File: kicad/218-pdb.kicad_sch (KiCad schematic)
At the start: 73 parts, among them J1 Conn_01x03, J10 Conn_01x03, J11 Conn_01x03, J12 Conn_01x03, J13 Conn_01x03, J14 Conn_01x03, J15 Conn_01x03, J16 Conn_01x03, J17 Conn_01x03, J18 Conn_01x03, J19 Conn_01x03, J2 Conn_01x03, J20 Conn_01x03, J21 Conn_01x03, J22 Conn_01x03, J23 Conn_01x03, J24 Conn_01x03, J25 Conn_01x04_Pin, J26 Conn_01x04_Pin, J27 Conn_01x04_Pin, J28 Conn_01x04_Pin, J29 14 V molex, J3 Conn_01x03, J30 14 V molex, J31 14 V molex, J32 14 V molex, J33 external 5V, J34 battery, J35 battery, J4 Conn_01x03, J5 Conn_01x03, J6 Conn_01x03, J7 Conn_01x03, J8 Conn_01x03, J9 Conn_01x03, SW1 5V switch, U1 DC-DC buck, U2 DC-DC buck, U3 LD1117V33, U4 LD1117V33

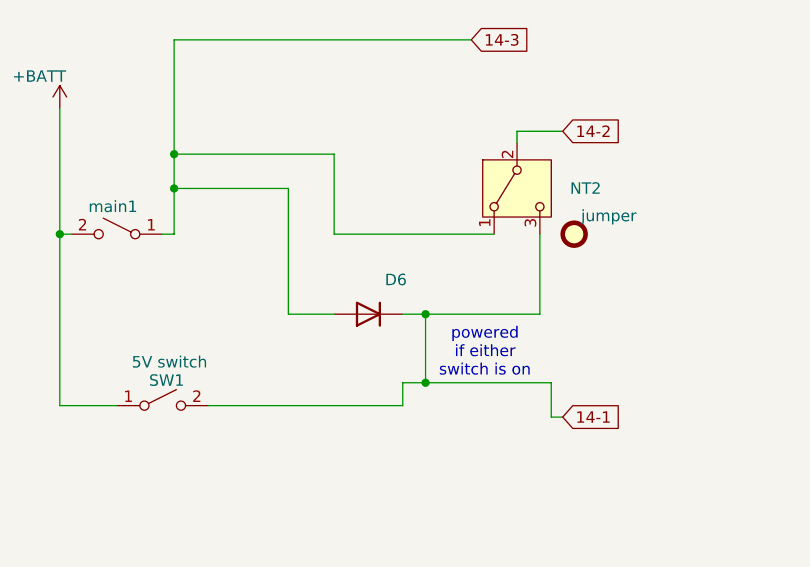
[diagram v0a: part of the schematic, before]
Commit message: change diode
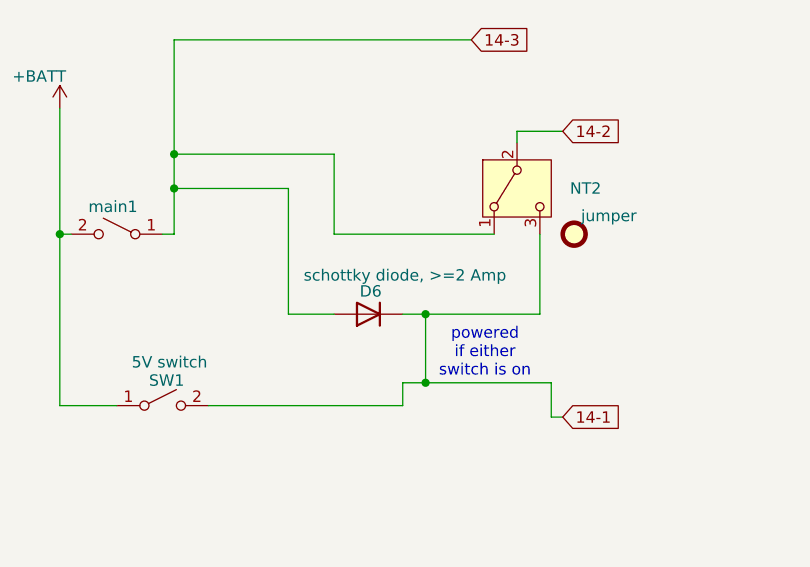
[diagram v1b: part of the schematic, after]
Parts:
- D6: value diode, >=1Amp -> schottky diode, >=2 Amp; Part_Number spdl, 1N4935 -> >=2 Amp schottky e.g. SB260S-E3/54 digikey 112-SB260S-E3/54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
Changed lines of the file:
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@@
 		(dnp no)
 		(property "Reference" "D6"
-			(at 91.948 137.16 0)
+			(at 89.154 138.43 0)
 			(effects
 				(font
@@
 			)
 		)
-		(property "Value" "diode, >=1Amp"
-			(at 88.9 137.16 0)
+		(property "Value" "schottky diode, >=2 Amp"
+			(at 92.964 136.652 0)
 			(effects
 				(font
 					(size 1.27 1.27)
 				)
-				(hide yes)
 			)
 		)
@@
 			)
 		)
-		(property "Description" "Diode"
+		(property "Description" ""
 			(at 88.9 140.97 0)
 			(effects
@@
 			)
 		)
-		(property "Part_Number" "spdl, 1N4935"
+		(property "Part_Number" ">=2 Amp schottky e.g. SB260S-E3/54 digikey 112-SB260S-E3/54CT-ND"
 			(at 88.9 140.97 0)
 			(effects

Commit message: start diagram
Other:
- moved on the sheet: D3, D4, D5, D6, J29, J30, J31, J32, J33, J34, J35, NT1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

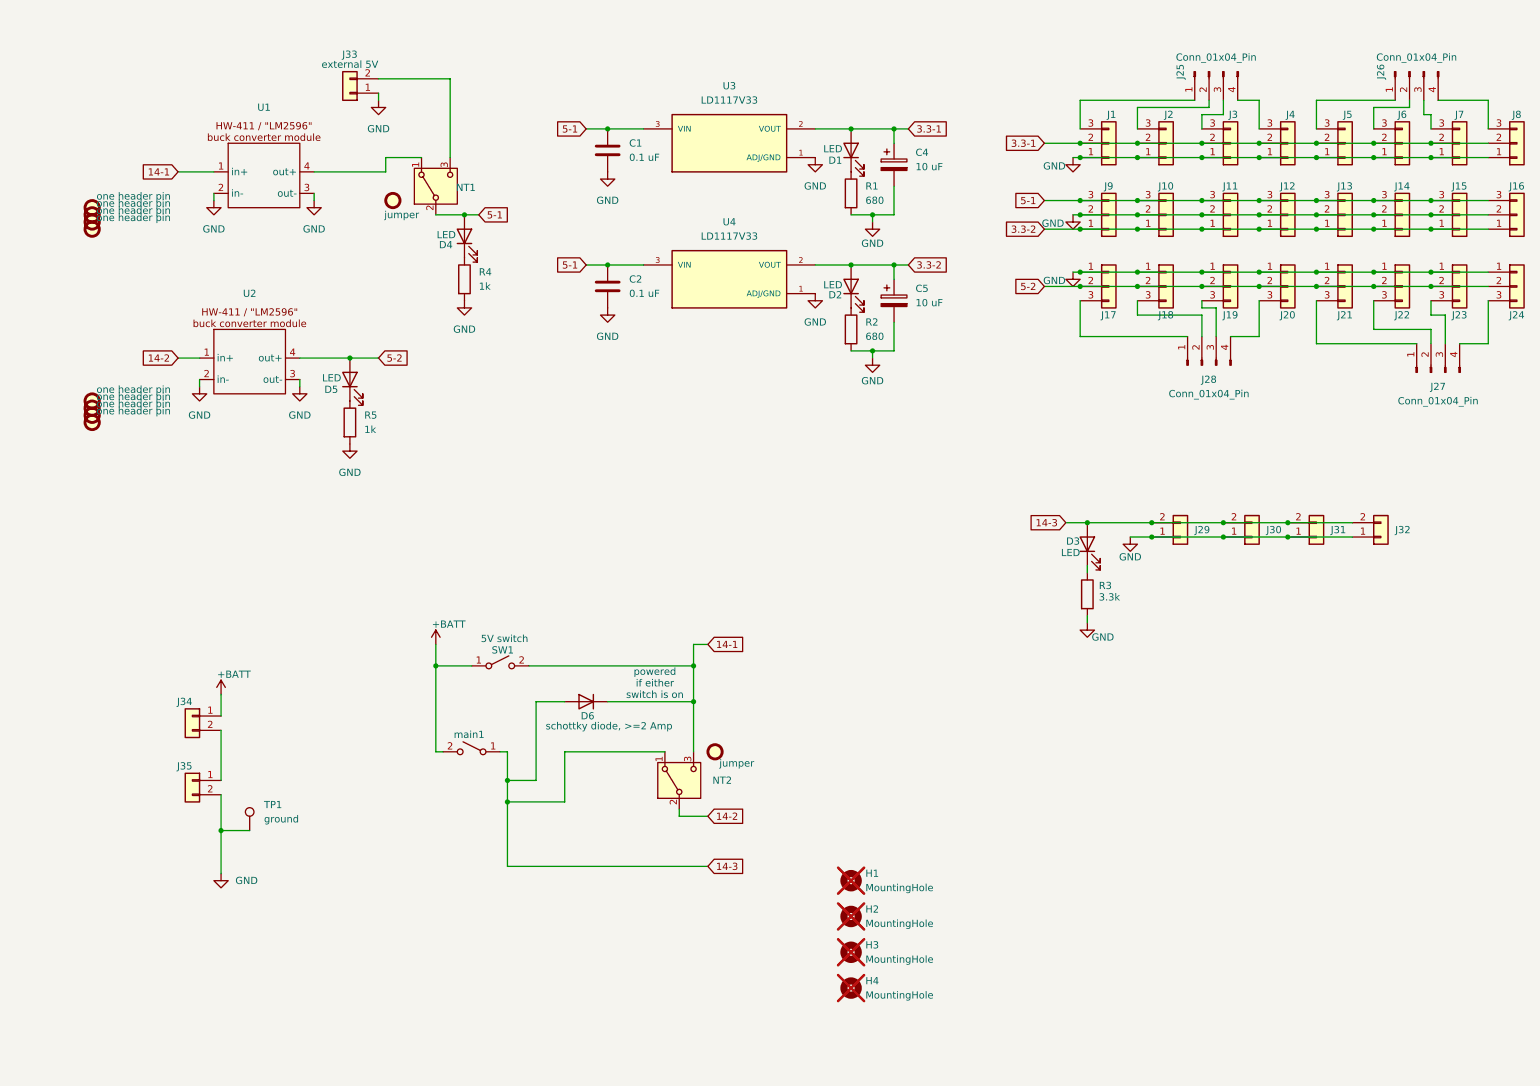
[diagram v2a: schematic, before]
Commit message: change diode
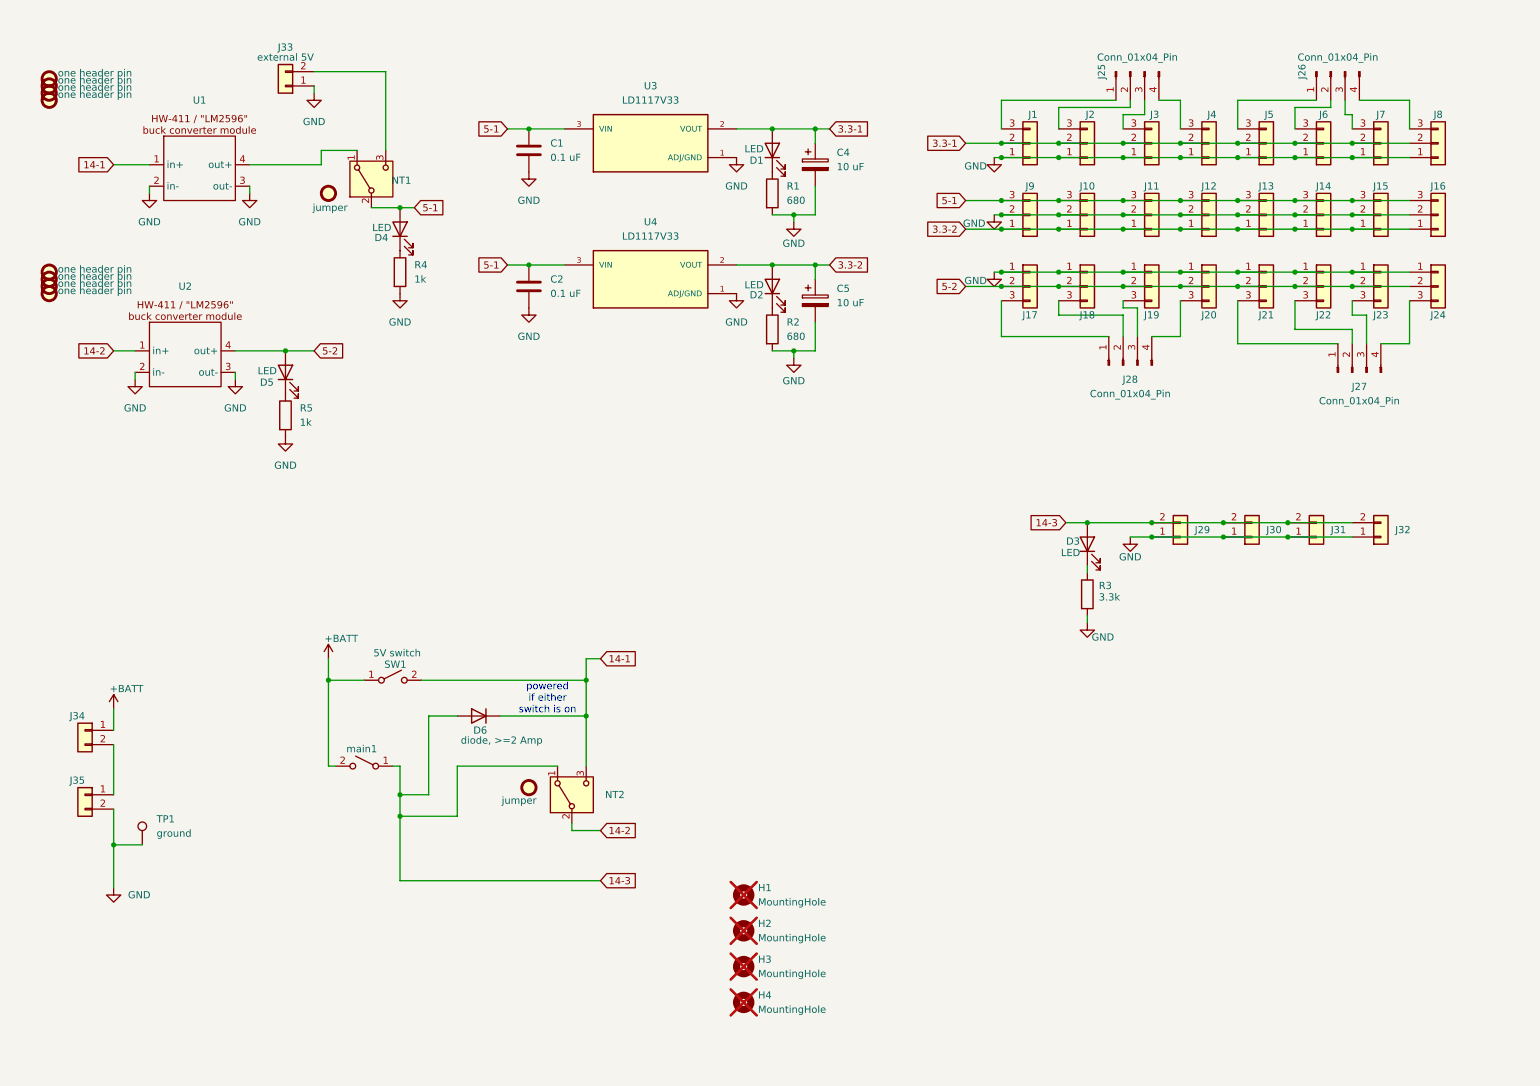
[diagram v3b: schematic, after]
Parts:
- D6: value schottky diode, >=2 Amp -> diode, >=2 Amp; footprint Diode_THT:D_DO-41_SOD81_P2.54mm_Vertical_AnodeUp -> Diode_THT:D_DO-15_P2.54mm_Vertical_AnodeUp; Part_Number >=2 Amp schottky e.g. SB260S-E3/54 digikey 112-SB260S-E3/54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 -> >=2 Amp diode, e.g. Diotec 1N5060
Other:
- company: SPDL -> (none)
- title: 218-PDB -> SPDL PCB
- moved on the sheet: C1, C2, C4, C5, D1, D2, D4, D5, D6, H1, H2, H3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

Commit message: update silkscreen
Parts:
- main1: value MotorSW -> MainSW
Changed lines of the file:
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@@
 			)
 		)
-		(property "Value" "MotorSW"
+		(property "Value" "MainSW"
 			(at 72.39 151.13 0)
 			(effects

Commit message: restart
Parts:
- removed FID3, FID4, FID5, FID6: one header pin, 218-pdb:PinHeader_1x01_P2.54mm_Vertical, symbol Mechanical:Fiducial
- removed J25, J26: Conn_01x04_Pin, Connector_PinHeader_2.54mm:PinHeader_1x04_P2.54mm_Vertical, symbol Connector:Conn_01x04_Pin
- removed J32: 14 V molex, 218-pdb:Molex_KK-396_A-41791-0002_1x02_P3.96mm_Vertical, symbol 218-pdb:Conn_01x02
- added J28: battery, 218-pdb:CUI_TB007-508-02BE, symbol 218-pdb:Conn_01x02
- added U5: LD1117V50, 218-pdb:TO255P1020X450X1968-3, symbol 218-pdb:LD1117V33
- FID1: renamed from FID7; value one header pin -> one 90 degree header pin; footprint 218-pdb:PinHeader_1x01_P2.54mm_Vertical -> 218-pdb:PinHeader_1x01_P2.54mm_H; Part_Number spdl, one header pin -> (none)
- FID2: renamed from FID8; value one header pin -> one 90 degree header pin; footprint 218-pdb:PinHeader_1x01_P2.54mm_Vertical -> 218-pdb:PinHeader_1x01_P2.54mm_H; Part_Number spdl, one header pin -> (none)
- FID3: renamed from FID9; value one header pin -> one 90 degree header pin; footprint 218-pdb:PinHeader_1x01_P2.54mm_Vertical -> 218-pdb:PinHeader_1x01_P2.54mm_H; Part_Number spdl, one header pin -> (none)
- FID4: renamed from FID10; value one header pin -> one 90 degree header pin; footprint 218-pdb:PinHeader_1x01_P2.54mm_Vertical -> 218-pdb:PinHeader_1x01_P2.54mm_H; Part_Number spdl, one header pin -> (none)
- J1, J10, J11, J12, J13, J14, J15, J16, J2, J3, J4, J5, J6, J7, J8, J9: footprint 218-pdb:Molex_KK-254_AE-6410-03A_1x03_P2.54mm_Vertical -> 218-pdb:JST_XH_B3B-XH-A_1x03_P2.50mm_Vertical; Part_Number 3 pin KK254 molex 0022232031 -> 3 pin JST XH
- J29, J30, J31: value 14 V molex -> battery; footprint 218-pdb:Molex_KK-396_A-41791-0002_1x02_P3.96mm_Vertical -> 218-pdb:CUI_TB007-508-02BE; Part_Number 2 pin KK396 molex 0026604020 -> screw terminal, 5.08" pitch, TB007-508-02BE
- renumbered C4 to C2, C2 to C3, C5 to C4, D5 to D2, D2 to D3, D3 to D5, FID1 to FID10, FID2 to FID9, J28 to J25, J27 to J26, J33 to J27, J34 to J32, J35 to J33, R5 to R2, R2 to R3, R3 to R5, U3 to U1, U4 to U3, U1 to U4
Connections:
- net 14-3: now also J28.2 (Pin_2)
- net 3.3-1: now also J1.1 (Pin_1), J2.1 (Pin_1), J3.1 (Pin_1), J4.1 (Pin_1), J5.1 (Pin_1), J6.1 (Pin_1), J7.1 (Pin_1), J8.1 (Pin_1); no longer J1.2 (Pin_2), J2.2 (Pin_2), J3.2 (Pin_2), J4.2 (Pin_2), J5.2 (Pin_2), J6.2 (Pin_2), J7.2 (Pin_2), J8.2 (Pin_2)
- net 5-1: now also J1.3 (Pin_3), J2.3 (Pin_3), J3.3 (Pin_3), J4.3 (Pin_3), J5.3 (Pin_3), J6.3 (Pin_3), J7.3 (Pin_3), J8.3 (Pin_3), U5.2 (VOUT); no longer NT1.2 (B)
- net GND: now also J1.2 (Pin_2), J2.2 (Pin_2), J3.2 (Pin_2), J4.2 (Pin_2), J5.2 (Pin_2), J6.2 (Pin_2), J7.2 (Pin_2), J8.2 (Pin_2), J28.1 (Pin_1), U5.1 (ADJ/GND); no longer J1.1 (Pin_1), J2.1 (Pin_1), J3.1 (Pin_1), J4.1 (Pin_1), J5.1 (Pin_1), J6.1 (Pin_1), J7.1 (Pin_1), J8.1 (Pin_1)
- new net: NT1.2 (B), U5.3 (VIN)
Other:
- moved on the sheet: D2, D4, D6, J27, NT1, NT2, R2, R4, SW1, U2, U4, main1

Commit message: start design E
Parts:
- added C5: 10 uF, Capacitor_THT:C_Disc_D3.8mm_W2.6mm_P2.50mm, symbol Device:C_Polarized
- added C6: 0.1 uF, Capacitor_THT:C_Disc_D3.0mm_W2.0mm_P2.50mm, symbol Device:C
- added TP2, TP3: TestPoint, symbol Connector:TestPoint
- SW1: footprint 218-pdb:SLW-12689-4A-N-D -> (none); Part_Number SLW-12689-4A-N-D -> ANT11SF1CQE
- U1, U3: value LD1117V33 -> 3.3V 0.5A LDO; footprint 218-pdb:TO255P1020X450X1968-3 -> Package_TO_SOT_THT:TO-220-3_Vertical; Part_Number LD1117V33 -> MCP1825S-3302E/AB
- U5: value LD1117V50 -> 5V 1.0A LDO; footprint 218-pdb:TO255P1020X450X1968-3 -> Package_TO_SOT_THT:TO-220-3_Vertical; Check_prices https://www.snapeda.com/parts/LD1117V33/STMicroelectronics/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 -> (none); Description_1 Linear Voltage Regulator IC Positive Fixed 1 Output 800mA T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 -> (none); DigiKey_Part_Number 497-1491-5-ND -> (none); MANUFACTURER ST Microelectronics -> (none); MAXIMUM_PACKAGE_HEIGHT 19.68mm -> (none); MF STMicroelectronics -> (none); MP LD1117V33 -> (none); Manufacturer_Name STMicroelectronics -> (none); PARTREV 37 -> (none); Package TO-220 STMicroelectronics -> (none); Part_Number LD1117V33 -> MCP1826S-5002E/AB; STANDARD IPC-7351B -> (none); SnapEDA_Link https://www.snapeda.com/parts/LD1117V33/STMicroelectronics/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 -> (none); digikey_part_number 497-1491-5-ND -> (none)
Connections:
- net 3.3-1: now also J1.3 (Pin_3), J2.3 (Pin_3), J3.3 (Pin_3), J4.3 (Pin_3), J5.3 (Pin_3), J6.3 (Pin_3), J7.3 (Pin_3), J8.3 (Pin_3); no longer J1.1 (Pin_1), J2.1 (Pin_1), J3.1 (Pin_1), J4.1 (Pin_1), J5.1 (Pin_1), J6.1 (Pin_1), J7.1 (Pin_1), J8.1 (Pin_1)
- net 3.3-2: now also J10.3 (Pin_3), J11.3 (Pin_3), J12.3 (Pin_3), J13.3 (Pin_3), J14.3 (Pin_3), J15.3 (Pin_3), J16.3 (Pin_3), J9.3 (Pin_3); no longer J10.1 (Pin_1), J11.1 (Pin_1), J12.1 (Pin_1), J13.1 (Pin_1), J14.1 (Pin_1), J15.1 (Pin_1), J16.1 (Pin_1), J9.1 (Pin_1)
- net 5-1: now also J1.1 (Pin_1), J10.1 (Pin_1), J11.1 (Pin_1), J12.1 (Pin_1), J13.1 (Pin_1), J14.1 (Pin_1), J15.1 (Pin_1), J16.1 (Pin_1), J2.1 (Pin_1), J3.1 (Pin_1), J4.1 (Pin_1), J5.1 (Pin_1), J6.1 (Pin_1), J7.1 (Pin_1), J8.1 (Pin_1), J9.1 (Pin_1), NT1.2 (B); no longer J1.3 (Pin_3), J10.3 (Pin_3), J11.3 (Pin_3), J12.3 (Pin_3), J13.3 (Pin_3), J14.3 (Pin_3), J15.3 (Pin_3), J16.3 (Pin_3), J2.3 (Pin_3), J3.3 (Pin_3), J4.3 (Pin_3), J5.3 (Pin_3), J6.3 (Pin_3), J7.3 (Pin_3), J8.3 (Pin_3), J9.3 (Pin_3), U5.2 (VOUT)
- net 5-2: now also TP2.1
- net GND: now also C5.2, C6.2
- net at U4.4 (out+): now also U5.3 (VIN), C6.1, TP3.1; no longer NT1.1 (A)
- new net: C5.1, NT1.1 (A), U5.2 (VOUT)
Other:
- note added: "update LDO part and pinout"
- moved on the sheet: D4, J27, NT1, R4, U5
